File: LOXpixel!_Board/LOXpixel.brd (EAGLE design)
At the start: 100 x 35.5 mm, 18 parts, among them IC2 7805T, Q1 BSS138, Q2 BSS138

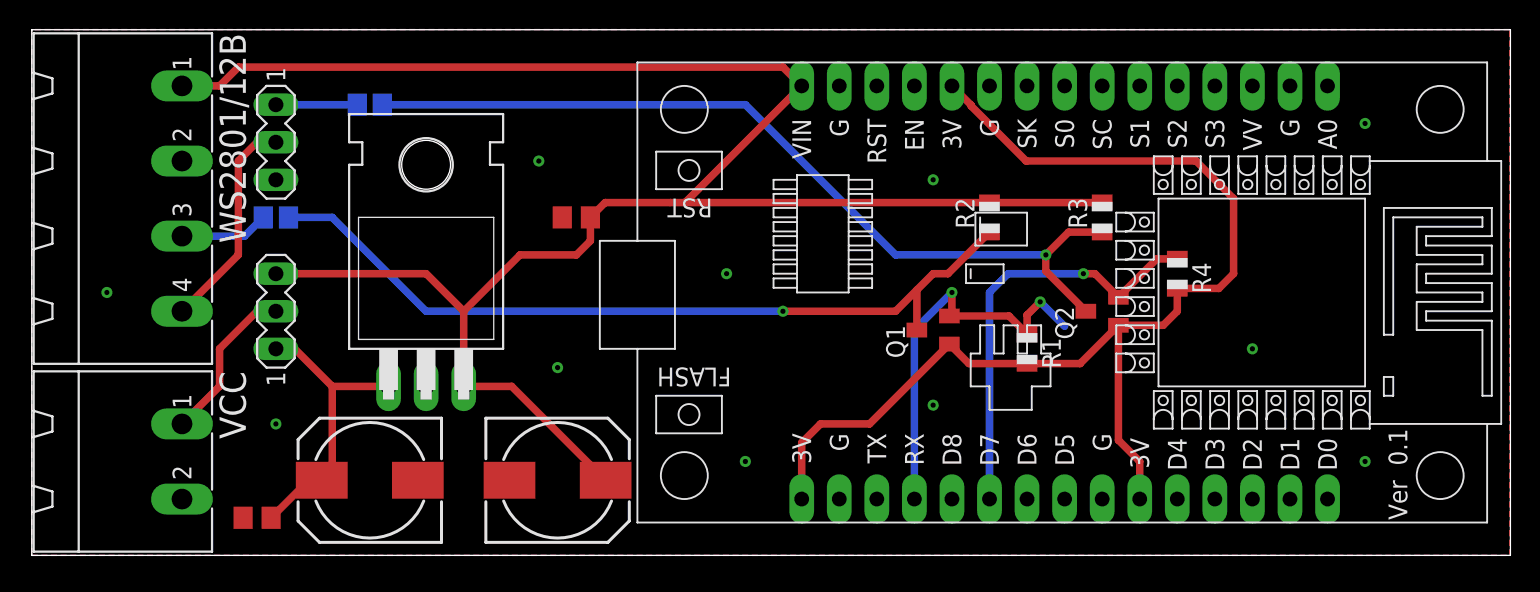
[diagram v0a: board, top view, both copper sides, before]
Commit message: pcb for hammond 1551usb3 and rebuild without nodemcu and for esp-wroom-02
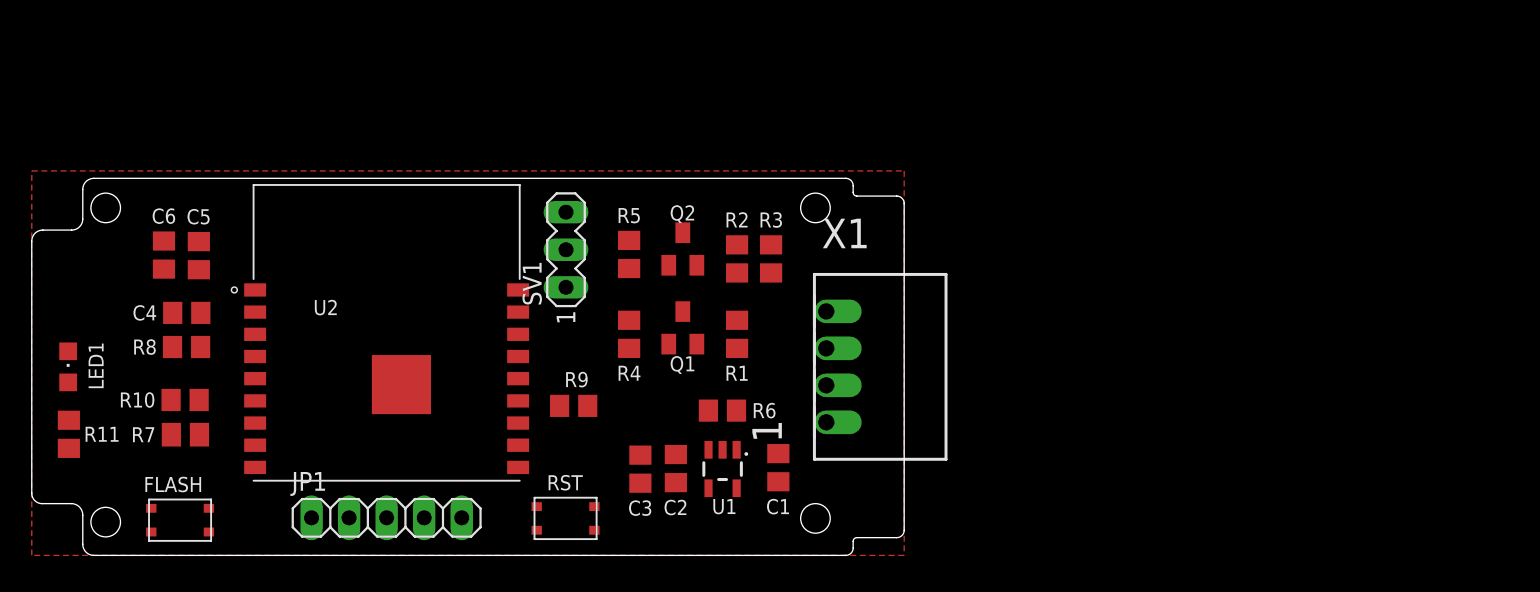
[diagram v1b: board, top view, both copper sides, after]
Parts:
- removed C14, C15: 100µF, rcl:150CLZ-0810
- removed C16, C17: 100n, rcl:C0805
- removed IC2: 7805T, linear:TO220H
- removed SV2: (no value), con-lstb:MA03-1
- removed U$1: NODEMCU, nodemcu:NODEMCU
- removed VCC: MSTBA2, con-phoenix-508:MSTBA2
- removed WS2801/12B: MSTBA4, con-phoenix-508:MSTBA4
- added C1, C2, C6: 10µ, rcl:C0805
- added C3: 1µ, rcl:C0805
- added C4, C5: 100n, rcl:C0805
- added FLASH, RST: KMR231, eagle-book:GLFS
- added JP1: (no value), pinhead:1X05
- added LED1: (no value), led:CHIPLED_0805
- added R10, R6, R9: 10k, rcl:R0805
- added R11: 1k, rcl:R0805
- added R5: 10K, rcl:R0805
- added U1: AP2112K, SparkFun-IC-Power:SOT23-5
- added U2: ESP-WROOM-02, ESP-WROOM-02:MODULE_ESP-WROOM-02
- added X1: 733-364, con-wago_2.5mm:P-733-364
- R1, R2, R4: device adafruit:R0805 -> rcl:R0805
- R3: value 10K -> 300; device adafruit:R0805 -> rcl:R0805
- R7: value 300 -> 10k; device rcl:R0805 -> rcl:M0805
- R8: value 300 -> 10k
- moved R4 37.3 mm to (40.4, 14.9)
- moved Q2 28.7 mm to (44.0, 20.7), turned to 0 degrees
- moved R3 22.6 mm to (50.0, 20.1)
- moved R8 20.5 mm to (10.5, 14.1), flipped to the top, turned to 180 degrees
- moved SV1 20.1 mm to (36.1, 20.7)
- moved R1 19.6 mm to (47.7, 14.9)
- moved R2 17.3 mm to (47.7, 20.1)
- moved Q1 16.9 mm to (44.0, 15.4), turned to 0 degrees
- moved R7 15.9 mm to (10.4, 8.16), flipped to the top
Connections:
- removed net 12VGLATT: C14.+, C16.1, IC2.1, SV1.1
- removed net N$11: Q2.2, R4.1, U$1.21
- removed net N$12: Q2.3, R3.1, R8.1
- removed net N$4: SV2.2, WS2801/12B.4
- removed net N$5: R8.2, SV2.1
- removed net N$6: R7.2, WS2801/12B.3
- removed net N$7: Q1.2, R1.1, U$1.19
- removed net N$8: Q1.3, R2.1, R7.1
- new net BOOTMODE: R10.2, U2.6
- new net CHIPEN: C4.1, R8.1, U2.2
- new net CLK: Q2.2, R5.1, U2.5
- new net CLKD-5V: Q2.3, R2.1, R3.1
- new net DATA-5V: Q1.3, R1.1, X1.L2
- new net FLASH: FLASH.P$2, FLASH.P$4, R7.2, U2.8
- new net LEDCLK: SV1.2, X1.L3
- new net N$1: R6.2, U1.3
- new net N$10: R3.2, SV1.1
- new net RST: R9.1, RST.P$2, RST.P$4, U2.15
- new net RXD: JP1.4, Q1.2, R4.1, U2.11
- new net STATLED: R11.2, U2.4
- new net TXD: JP1.3, U2.12
- net +3V3: now also C2.2, C3.2, C5.1, C6.1, JP1.5, R5.2, R7.1, R8.2, R9.2, U1.5, U2.1; no longer R1.2, U$1.11, U$1.16, U$1.25
- net +5V: now also C1.2, R1.2, R6.1, U1.1, X1.L1; no longer C15.+, C17.1, IC2.3, R3.2, SV1.3, U$1.15, WS2801/12B.1
- net GND: now also C1.1, C2.1, C3.1, C4.2, C5.2, C6.2, FLASH.P$1, FLASH.P$3, JP1.2, LED1.C, R10.1, RST.P$1, RST.P$3, SV1.3, U1.2, U2.13, U2.18, U2.19, U2.9, X1.L4; no longer C14.-, C15.-, C16.2, C17.2, IC2.2, SV2.3, U$1.10, U$1.14, U$1.17, U$1.2, U$1.24, VCC.2, WS2801/12B.2
- net N$2: now also LED1.A, R11.1; no longer SV1.2, VCC.1
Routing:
- net +5V: track 132.3 -> 0.00 mm
- net +3V3: track 79.4 -> 0.00 mm
- net N$12: track 58.5 -> 0.00 mm, vias 1 -> 0
- net N$8: track 55.0 -> 0.00 mm, vias 1 -> 0
- net N$11: track 28.9 -> 0.00 mm, vias 1 -> 0
- net N$7: track 27.2 -> 0.00 mm, vias 2 -> 0
- net 12VGLATT: track 20.3 -> 0.00 mm
- net N$4: track 14.8 -> 0.00 mm
- net N$2: track 11.0 -> 0.00 mm
- net N$6: track 6.03 -> 0.00 mm
- net N$5: track 5.50 -> 0.00 mm
- removed copper zone on layer 16, net GND
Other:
- board size 100 x 35.5 mm -> 59 x 25.5 mm
- board text removed: "[LOXpixel!]"
- board text removed: "www.unser-smartes-zuhause.de"

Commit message: finished first board revision
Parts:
- removed RST: KMR231, eagle-book:GLFS
- added RESET: KMR231, eagle-book:GLFS
- added U$1: (no value), codm:CODM-LOGO
- added U$2: (no value), codm:WEEE-LOGO-5MM
- added U$3: (no value), oshw:OSHW_5MM
- R7: device rcl:M0805 -> rcl:R0805
- moved SV1 14.5 mm to (48.2, 12.5), turned to 270 degrees
- moved Q2 7.88 mm to (38.8, 14.9), turned to 270 degrees
- moved R3 7.57 mm to (44.5, 14.8), turned to 270 degrees
- moved R5 7.50 mm to (35.3, 14.8), turned to 90 degrees
- moved R2 7.50 mm to (42.3, 14.8), turned to 270 degrees
- moved Q1 5.75 mm to (41.0, 10.5), turned to 270 degrees
- moved R6 5.60 mm to (47.0, 4.20), turned to 270 degrees
- moved R1 5.52 mm to (44.5, 10.4), turned to 90 degrees
- moved R4 5.35 mm to (37.5, 10.4), turned to 90 degrees
- moved C2 3.26 mm to (40.8, 4.20)
- moved U1 3.24 mm to (43.9, 4.20)
- moved C3 3.15 mm to (38.5, 4.20)
- moved C1 2.16 mm to (49.2, 4.20)
- moved JP1 2.04 mm to (22.0, 2.94)
- moved U2 2.00 mm to (22.0, 13.1)
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- renumbered LED1 to STATUS
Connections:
- net CLKD-5V renamed CLK-5V
- net GND: now also RESET.P$1, RESET.P$3; no longer RST.P$1, RST.P$3
- net RST: now also RESET.P$2, RESET.P$4; no longer RST.P$2, RST.P$4
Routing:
- net +3V3: track 0.00 -> 98.0 mm, vias 0 -> 5
- net CLK: track 0.00 -> 25.4 mm, vias 0 -> 2
- net +5V: track 0.00 -> 22.9 mm
- net RXD: track 0.00 -> 21.6 mm
- net RST: track 0.00 -> 17.2 mm, vias 0 -> 2
- net DATA-5V: track 0.00 -> 17.1 mm, vias 0 -> 1
- net STATLED: track 0.00 -> 15.1 mm
- net TXD: track 0.00 -> 12.8 mm
- net FLASH: track 0.00 -> 11.0 mm
- net LEDCLK: track 0.00 -> 6.17 mm
- net N$1: track 0.00 -> 5.36 mm
- net CHIPEN: track 0.00 -> 4.99 mm
- net N$10: track 0.00 -> 4.15 mm
- net CLK-5V: track 0.00 -> 2.84 mm
- net BOOTMODE: track 0.00 -> 2.68 mm
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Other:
- board text added: "1-2"
- board text added: "2-3"
- board text added: "3V3"
- board text added: "90060-0.1"
- board text added: "GND"
- board text added: "LoxPixel V0.1, codm.de 2019 CC-BY-NC-SA"
- board text added: "Pixeltype"
- board text added: "RX"
- board text added: "TX"
- board text added: "Thank you for the idea, Dennis. www.unser-smartes-zuhause.de"
- board text added: "WS2801"
- board text added: "WS2812B"
